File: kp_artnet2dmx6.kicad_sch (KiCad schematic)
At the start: 65 parts, among them IC1 KSZ8081MNXIA-TR, IC2 M95640-RMN6P, J1 RJ45_Amphenol_RJMG1BD3B8K1ANR, J2 SCREEN, J3 Conn_01x06, J4 Conn_01x06, J5 Conn_01x06, J6 Conn_01x06, SW1 SW_SPDT, U1 STM32F407VETx, U2 MCP23S17_SP, U3 TCA9517ADGK, Y1 ASDDV-25.000MHZ-LC-T

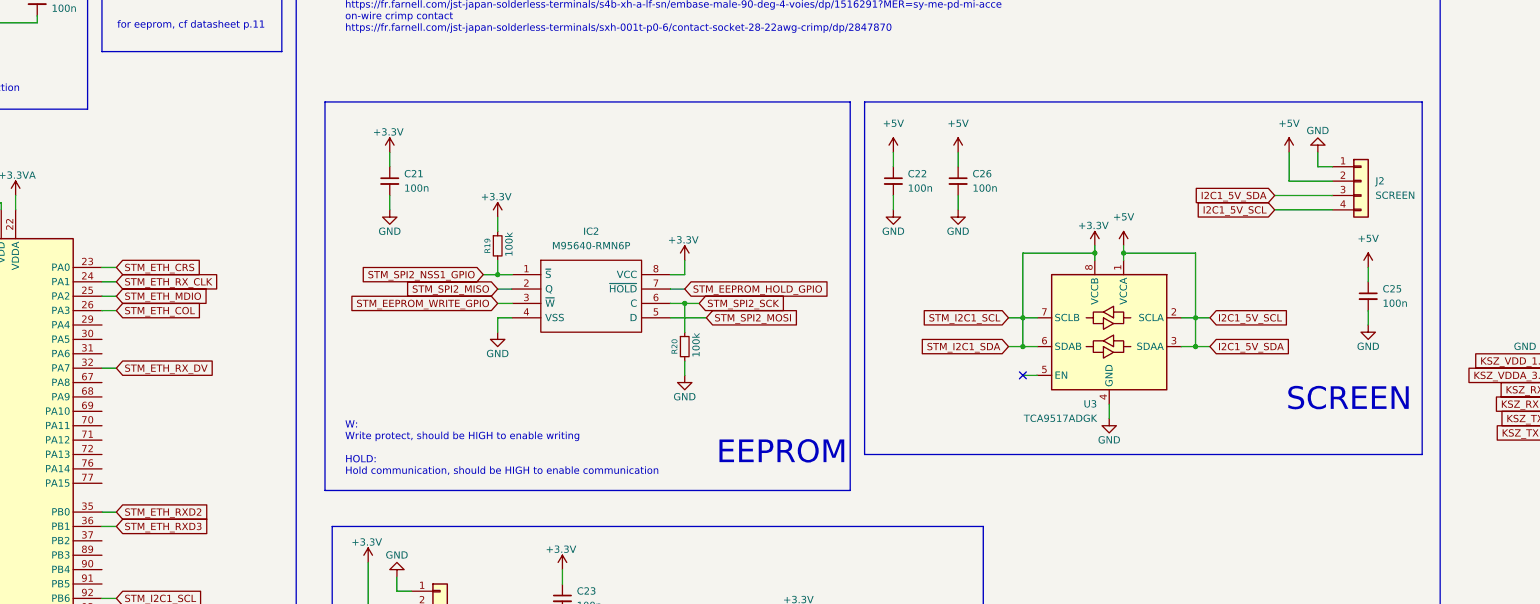
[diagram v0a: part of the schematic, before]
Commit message: use delayed 5v supply, add dmxinout board
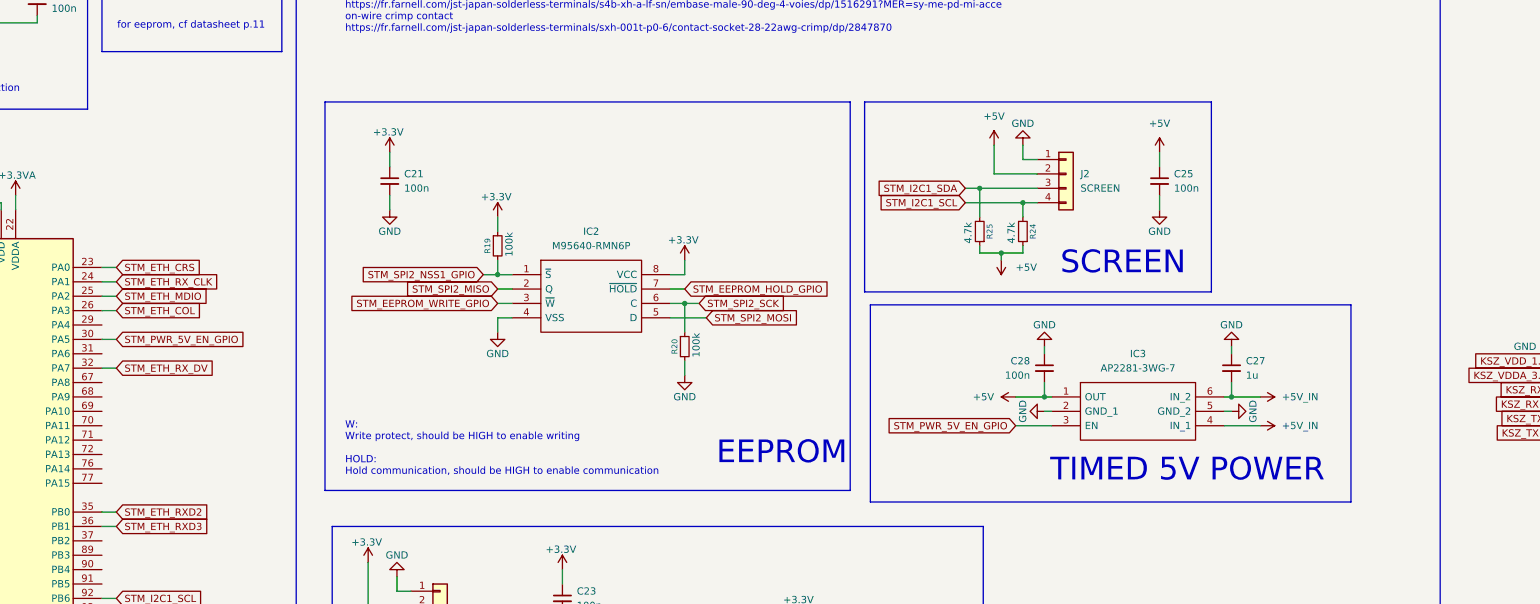
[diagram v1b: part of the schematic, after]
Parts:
- removed C22, C26: 100n, symbol Device:C_Small
- removed U3: TCA9517ADGK, Package_SO:VSSOP-8_3x3mm_P0.65mm, symbol Logic_LevelTranslator:TCA9517ADGK
- added C27: 1u, symbol Device:C_Small
- added C28: 100n, symbol Device:C_Small
- added IC3: AP2281-3WG-7, SOT95P285X140-6N, symbol SamacSys:AP2281-3WG-7
- added R24, R25: 4.7k, symbol Device:R_Small
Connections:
- net +3.3V: no longer U1.92 (PB6), U1.93 (PB7)
- net +5V: now also C28.2, IC3.1 (OUT), R24.1, R25.1; no longer J2.3 (Pin_3), J2.4 (Pin_4)
- net GND: now also C27.1, C28.1, IC3.2 (GND_1), IC3.5 (GND_2)
- net STM_PWR_5V_EN_GPIO: now reaches U1.30 (PA5)
- net STM_PWR_5V_EN_GPIO: now also IC3.3 (EN)
- new net +5V_IN: C27.2, IC3.4 (IN_1), IC3.6 (IN_2)
- new net STM_I2C1_SCL: J2.4 (Pin_4), R24.2, U1.92 (PB6)
- new net STM_I2C1_SDA: J2.3 (Pin_3), R25.2, U1.93 (PB7)
- no-connect marks 4 -> 3
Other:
- note added: "TIMED 5V POWER"
- moved on the sheet: C25, J2

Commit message: connect usb
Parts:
- added C22, C26, C29, C30, C31, C32: 100n, symbol Device:C_Small
- added F1: 3A, symbol Device:Polyfuse_Small
- added FB4: 600@100MHz, Inductor_SMD:L_1206_3216Metric, symbol Device:FerriteBead_Small
- added H1, H2, H3: tooling, MountingHole:ToolingHole_1.152mm, symbol Mechanical:MountingHole
- added H4, H5, H6, H7: M3, MountingHole:MountingHole_3.2mm_M3_Pad_Via, symbol Mechanical:MountingHole_Pad
- added J10, J11, J12, J7, J8, J9: DMX, symbol Connector_Generic:Conn_01x04
- added J13: USB_B, symbol Connector:USB_B
- added Q1: AO3401A, Package_TO_SOT_SMD:SOT-23, symbol Transistor_FET:AO3401A
- added TP1: testpoint, TestPoint:TestPoint_THTPad_1.5x1.5mm_Drill0.7mm, symbol Connector:TestPoint_Small
- added U3: USBLC6-2SC6, Package_TO_SOT_SMD:SOT-23-6, symbol Power_Protection:USBLC6-2SC6
- FB1, FB2, FB3, FB5: JLCPCB Part # (none) -> C2858472
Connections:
- net +5V: now also C22.1, C26.1, C29.1, C30.1, C31.1, C32.1, J10.2 (Pin_2), J11.2 (Pin_2), J12.2 (Pin_2), J7.2 (Pin_2), J8.2 (Pin_2), J9.2 (Pin_2)
- net +5V_IN: now also FB4.2
- net GND: now also C22.2, C26.2, C29.2, C30.2, C31.2, C32.2, J10.1 (Pin_1), J11.1 (Pin_1), J12.1 (Pin_1), J13.4 (GND), J7.1 (Pin_1), J8.1 (Pin_1), J9.1 (Pin_1), Q1.1 (G), U3.2 (GND); no longer J1.R8, J1.SH
- net STM_USART3_TX: now reaches U1.55 (PD8)
- net STM_USART3_TX: now also J9.4 (Pin_4)
- net STM_USART3_RX: now reaches U1.56 (PD9)
- net STM_USART3_RX: now also J9.3 (Pin_3)
- net STM_USART6_TX: now reaches U1.63 (PC6)
- net STM_USART6_TX: now also J12.4 (Pin_4)
- net STM_USART6_RX: now reaches U1.64 (PC7)
- net STM_USART6_RX: now also J12.3 (Pin_3)
- net STM_USART1_TX: now reaches U1.68 (PA9)
- net STM_USART1_TX: now also J7.4 (Pin_4)
- net STM_USART1_RX: now reaches U1.69 (PA10)
- net STM_USART1_RX: now also J7.3 (Pin_3)
- net STM_UART4_TX: now reaches U1.78 (PC10)
- net STM_UART4_TX: now also J10.4 (Pin_4)
- net STM_UART4_RX: now reaches U1.79 (PC11)
- net STM_UART4_RX: now also J10.3 (Pin_3)
- net STM_UART5_TX: now reaches U1.80 (PC12)
- net STM_UART5_TX: now also J11.4 (Pin_4)
- net STM_UART5_RX: now reaches U1.83 (PD2)
- net STM_UART5_RX: now also J11.3 (Pin_3)
- net STM_USART2_TX: now reaches U1.86 (PD5)
- net STM_USART2_TX: now also J8.4 (Pin_4)
- net STM_USART2_RX: now reaches U1.87 (PD6)
- net STM_USART2_RX: now also J8.3 (Pin_3)
- new net: FB4.1, Q1.2 (S)
- new net: F1.2, Q1.3 (D)
- new net +5V_USB: F1.1, J13.1 (VBUS), U3.5 (VBUS)
- new net Earth: H4.1, H5.1, H6.1, H7.1, J1.R8, J1.SH, J13.5 (Shield)
- new net STM_USB_D+: U3.1 (I/O1)
- new net STM_USB_D-: U3.3 (I/O2)
- new net USB_D+: J13.3 (D+), U3.6 (I/O1)
- new net USB_D-: J13.2 (D-), U3.4 (I/O2)
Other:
- note added: "DMX"
- note added: "JLC tooling holes"
- note added: "USB"
- note added: "mounting holes"
- note added: "no need for USB D+ pull up for stm32f4xx see ST AN4879"

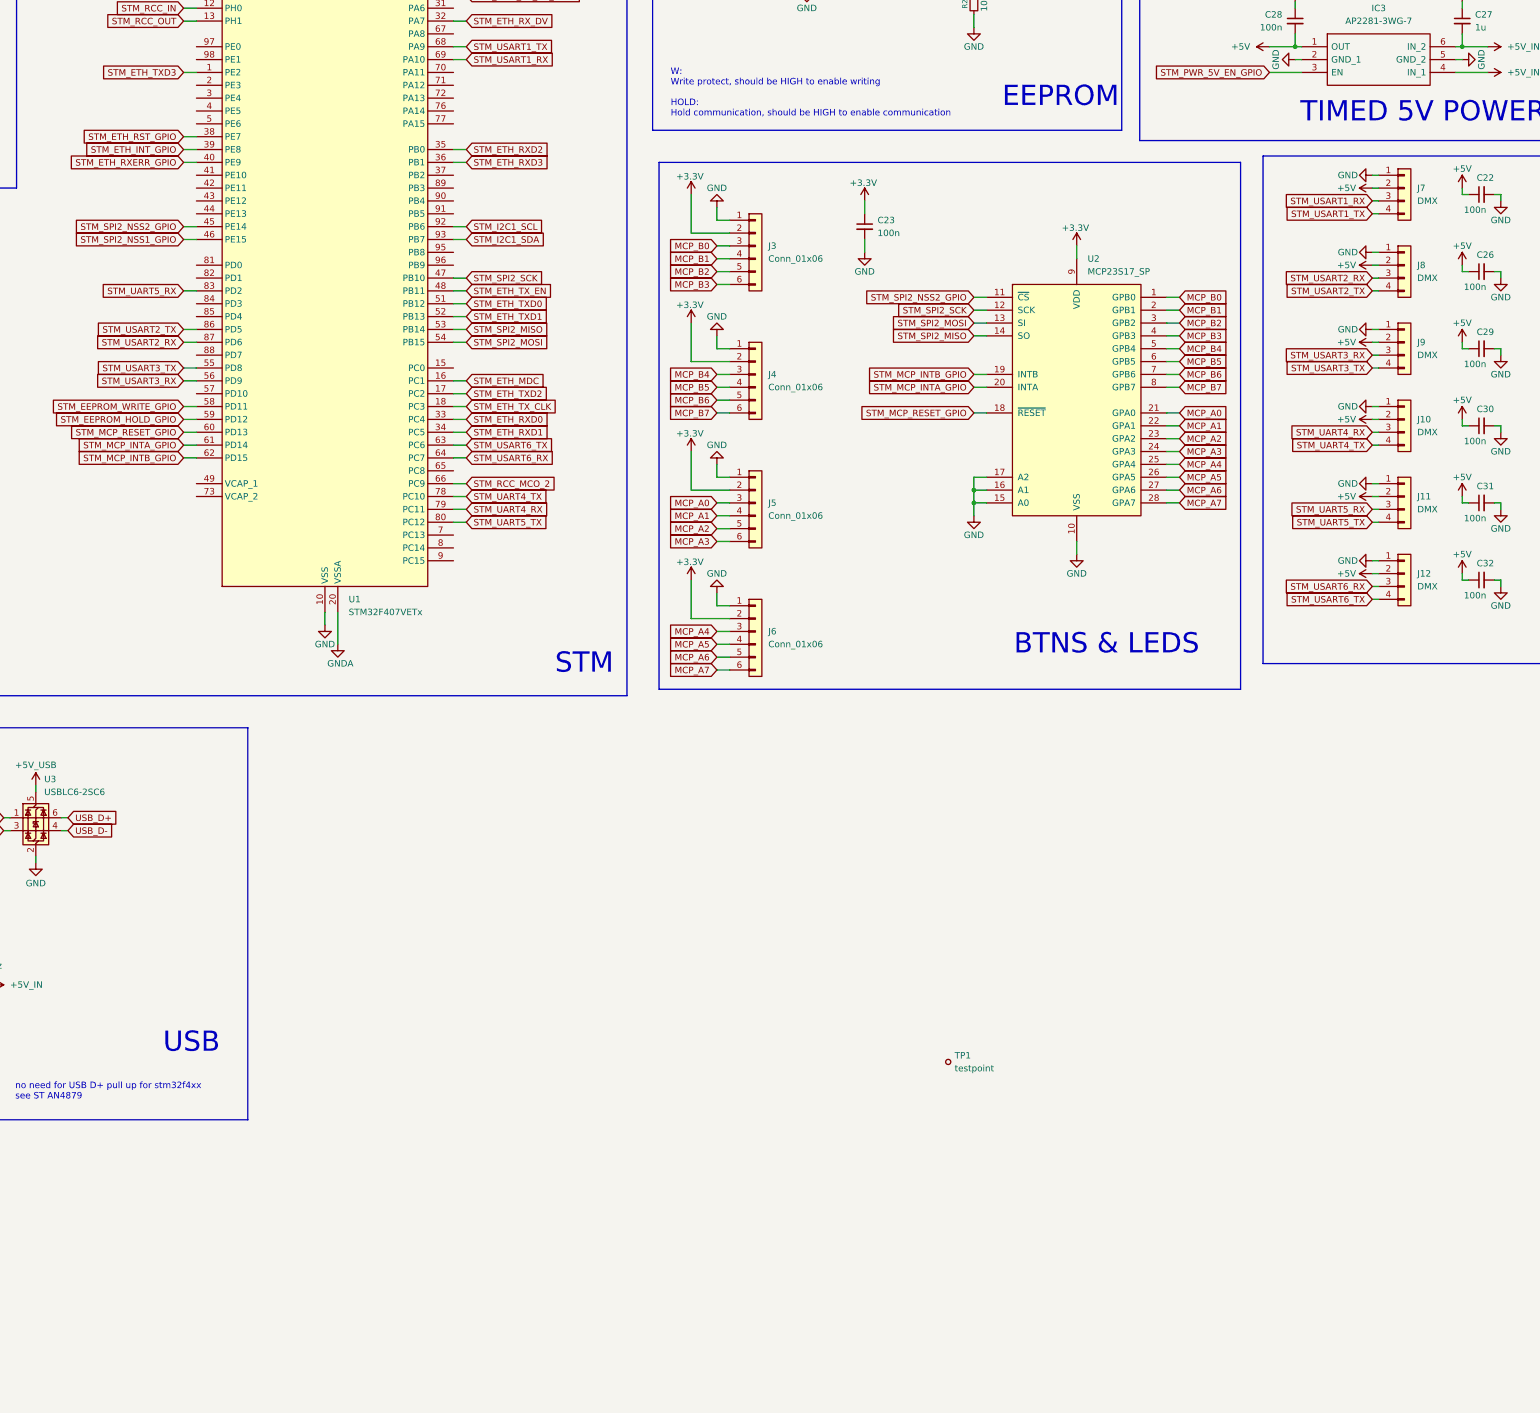
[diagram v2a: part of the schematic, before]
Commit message: sch: swd debug interface
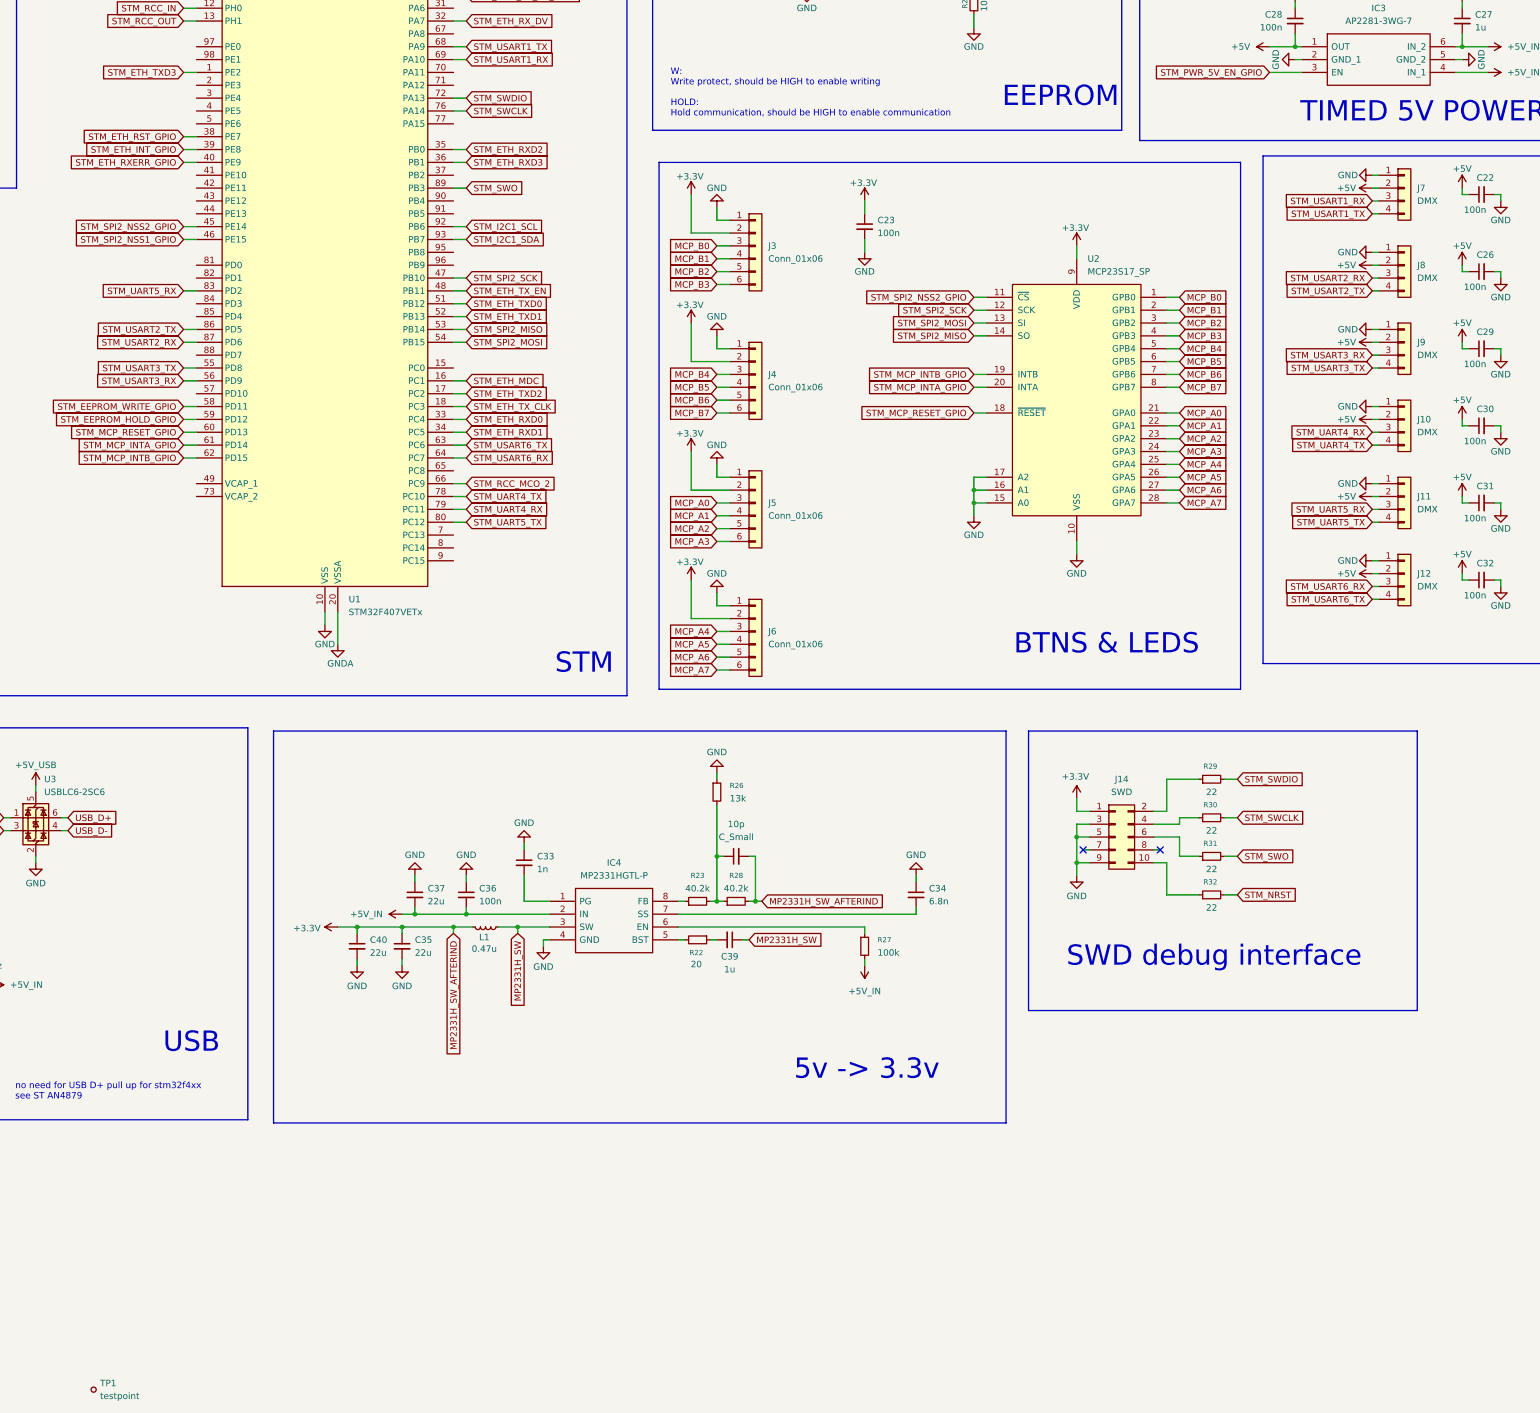
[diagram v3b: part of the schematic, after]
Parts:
- added 10p: C_Small, symbol Device:C_Small
- added C33: 1n, symbol Device:C_Small
- added C34: 6.8n, symbol Device:C_Small
- added C35, C37, C40: 22u, symbol Device:C_Small
- added C36: 100n, symbol Device:C_Small
- added C39: 1u, symbol Device:C_Small
- added IC4: MP2331HGTL-P, MP2331HGTLP, symbol SamacSys:MP2331HGTL-P
- added J14: SWD, Connector_PinSocket_1.27mm:PinSocket_2x05_P1.27mm_Vertical_SMD, symbol Connector_Generic:Conn_02x05_Odd_Even
- added L1: 0.47u, symbol Device:L_Small
- added R22: 20, symbol Device:R_Small
- added R23, R28: 40.2k, symbol Device:R_Small
- added R26: 13k, symbol Device:R_Small
- added R27: 100k, symbol Device:R_Small
- added R29, R30, R31, R32: 22, Resistor_SMD:R_0402_1005Metric, symbol Device:R_Small
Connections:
- net +3.3V: now also 10p.2, C35.1, C40.1, J14.1 (Pin_1), L1.2, R28.2
- net +5V_IN: now also C36.2, C37.2, IC4.2 (IN), R27.2
- net GND: now also C33.1, C34.1, C35.2, C36.1, C37.1, C40.2, IC4.4 (GND), J14.3 (Pin_3), J14.5 (Pin_5), J14.9 (Pin_9), R26.1
- net STM_NRST: now also R32.2
- net STM_SWDIO: now reaches U1.72 (PA13)
- net STM_SWDIO: now also R29.2
- net STM_SWCLK: now reaches U1.76 (PA14)
- net STM_SWCLK: now also R30.2
- net STM_SWO: now reaches U1.89 (PB3)
- net STM_SWO: now also R31.2
- new net: C39.2, R22.1
- new net: J14.4 (Pin_4), R30.1
- new net: IC4.5 (BST), R22.2
- new net: 10p.1, R23.2, R26.2, R28.1
- new net: C33.2, IC4.1 (PG)
- new net: IC4.6 (EN), R27.1
- new net: C34.2, IC4.7 (SS)
- new net: IC4.8 (FB), R23.1
- new net: J14.2 (Pin_2), R29.1
- new net: J14.10 (Pin_10), R32.1
- new net: J14.6 (Pin_6), R31.1
- new net MP2331H_SW: C39.1, IC4.3 (SW), L1.1
- no-connect marks 3 -> 5
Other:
- note added: "5v -> 3.3v"
- note added: "SWD debug interface"
- moved on the sheet: TP1

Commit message: footprints - the beginning
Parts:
- C1, C10, C11, C13, C15, C17, C19, C20, C21, C22, C23, C24, C25, C26, C28, C29, C3, C30, C31, C32, C33, C34, C36, C4, C5, C6, C7, C8: footprint (none) -> Capacitor_SMD:C_0402_1005Metric
- C12, C27, C39, C9: footprint (none) -> Capacitor_SMD:C_0805_2012Metric
- C14: value 10uF -> 10u; footprint (none) -> Capacitor_SMD:C_1206_3216Metric
- C16, C18, C2, C35, C37, C40: footprint (none) -> Capacitor_SMD:C_1206_3216Metric
- C38: renamed from 10p; value C_Small -> 10p; footprint (none) -> Capacitor_SMD:C_0402_1005Metric
- F1: footprint (none) -> Fuse:Fuse_1812_4532Metric; JLCPCB Part # (none) -> C18198349
- FB1, FB2, FB3, FB5: footprint (none) -> Inductor_SMD:L_1206_3216Metric
- IC1: footprint QFN50P500X500X100-33N-D -> SamacSys:QFN50P500X500X100-33N-D
- IC2: footprint SOIC127P600X175-8N -> SamacSys:SOIC127P600X175-8N
- IC3: footprint SOT95P285X140-6N -> SamacSys:SOT95P285X140-6N
- IC4: footprint MP2331HGTLP -> SamacSys:MP2331HGTLP
- J10, J11, J12, J7, J8, J9: footprint (none) -> Connector_JST:JST_XH_B4B-XH-A_1x04_P2.50mm_Vertical
- J13: footprint (none) -> SamacSys:USBBSRA; farnell link (none) -> https://fr.farnell.com/multicomp/usb-b-s-ra/conn-usb-2-0-ty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
- J3, J4, J5, J6: value Conn_01x06 -> BTN; footprint (none) -> Connector_IDC:IDC-Header_2x03_P2.54mm_Vertical
- L1: value 0.47u -> 470n; footprint (none) -> Inductor_SMD:L_0805_2012Metric; farnell link (none) -> https://fr.farnell.com/pulse-electronics/bdqq00201212r47mpa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
- R1: footprint (none) -> Resistor_SMD:R_0603_1608Metric
- Y1: footprint AbraconASDDV -> SamacSys:AbraconASDDV

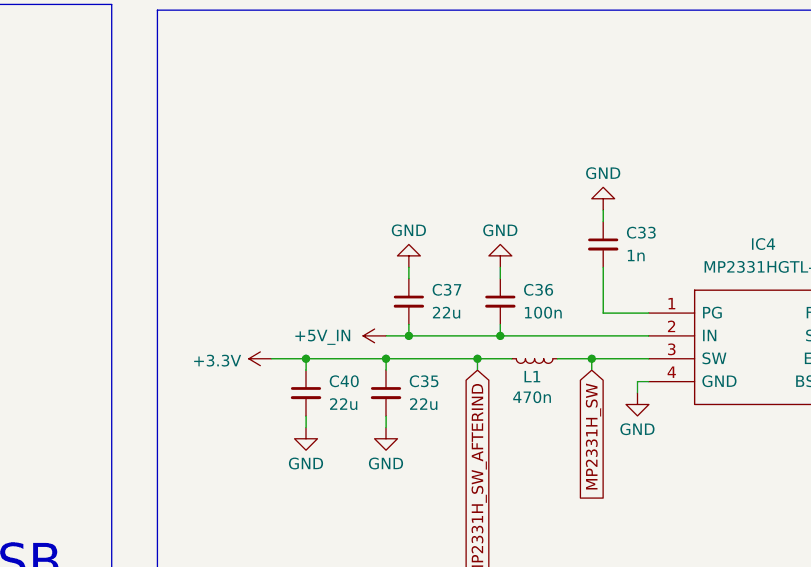
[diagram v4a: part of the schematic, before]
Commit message: all footprints assigned
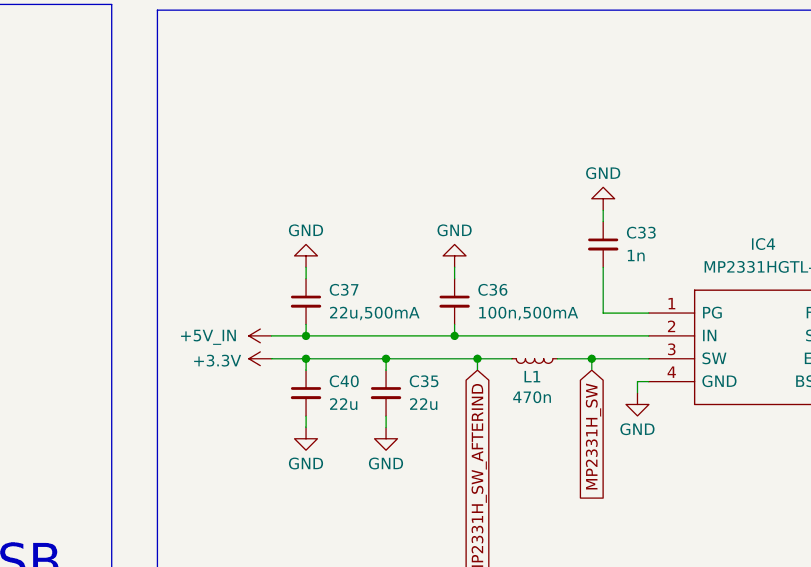
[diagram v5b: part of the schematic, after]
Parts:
- C16, C18, C35, C40: JLCPCB Part # (none) -> C5177178
- C36: value 100n -> 100n,500mA
- C37: value 22u -> 22u,500mA; JLCPCB Part # (none) -> C5177178
- R10, R11, R12, R13, R14, R15, R16, R17, R18, R19, R2, R20, R21, R22, R23, R24, R25, R26, R27, R28, R3, R4, R5, R6, R7, R8, R9: footprint (none) -> Resistor_SMD:R_0805_2012Metric
- R29, R30, R31, R32: footprint Resistor_SMD:R_0402_1005Metric -> Resistor_SMD:R_0805_2012Metric
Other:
- moved on the sheet: C36, C37

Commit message: fix usb conn
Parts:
- removed J13: USB_B, SamacSys:USBBSRA, symbol Connector:USB_B
- added J15: USB-B-S-RA, USBBSRA, symbol SamacSys:USB-B-S-RA
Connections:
- net +5V_USB: now also J15.2
- net Earth: now also J15.5, J15.6
- net GND: now also J15.4
- net MP2331H_SW: no longer IC4.3 (SW), L1.1
- net STM_USB_D+: now also U1.71 (PA12)
- net STM_USB_D-: now also U1.70 (PA11)
- net USB_D+: now also J15.3
- net USB_D-: now also J15.1
- new net: IC4.3 (SW), L1.1
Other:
- moved on the sheet: U3
